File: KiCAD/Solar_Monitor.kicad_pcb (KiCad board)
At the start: 2 copper layers, 40.6 x 22.9 mm, 15 parts, among them J1 Power IN, J2 Power Out, Q1 PN2222A, Q2 MCP102-300E/TO, U1 PIC16F15214-I/P

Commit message: Starting Rev: B
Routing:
- net Net-(C1-Pad1): track 59.3 -> 7.18 mm
- added copper zone on B.Cu, net Net-(C1-Pad1)
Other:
- board text added: "2022-02-16"
- board text added: "Rev: B"
- board text removed: "2022-02-15"
- board text removed: "Rev A"
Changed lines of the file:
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@@
   (net 9 "Net-(Q2-Pad1)")
   (net 10 "Net-(Q2-Pad2)")
-  (net 11 "Net-(U1-Pad7)")
+  (net 11 "Net-(Q1-Pad2)")
   (footprint "MountingHole:MountingHole_2.2mm_M2" (layer "F.Cu")
     (at 83.82 63.5)
@@
       (net 1 "Net-(D1-Pad1)") (pinfunction "Pin_1") (pintype "passive"))
     (pad "2" thru_hole oval (at 0 2.54) (size 1.7 1.7) (drill 1) (layers *.Cu *.Mask)
-      (net 2 "Net-(C1-Pad1)") (pinfunction "Pin_2") (pintype "passive"))
+      (net 2 "Net-(C1-Pad1)") (pinfunction "Pin_2") (pintype "power_out"))
     (model "${KICAD6_3DMODEL_DIR}/Connector_PinHeader_2.54mm.3dshapes/PinHeader_1x02_P2.54mm_Vertical.wrl"
       (offset (xyz 0 0 0))
@@
     (fp_line (start -0.635 -1.27) (end 1.27 -1.27) (layer "F.Fab") (width 0.1))
     (pad "1" thru_hole rect (at 0 0 180) (size 1.7 1.7) (drill 1) (layers *.Cu *.Mask)
-      (net 3 "Net-(C1-Pad2)") (pinfunction "Pin_1") (pintype "passive"))
+      (net 3 "Net-(C1-Pad2)") (pinfunction "Pin_1") (pintype "power_out"))
     (pad "2" thru_hole oval (at 0 2.54 180) (size 1.7 1.7) (drill 1) (layers *.Cu *.Mask)
-      (net 2 "Net-(C1-Pad1)") (pinfunction "Pin_2") (pintype "passive"))
+      (net 2 "Net-(C1-Pad1)") (pinfunction "Pin_2") (pintype "power_in"))
     (model "${KICAD6_3DMODEL_DIR}/Connector_PinHeader_2.54mm.3dshapes/PinHeader_1x02_P2.54mm_Vertical.wrl"
       (offset (xyz 0 0 0))
@@
     (fp_arc (start -0.483625 1.753625) (mid -1.021221 -0.949055) (end 1.27 -2.48) (layer "F.Fab") (width 0.1))
     (pad "1" thru_hole rect (at 0 0) (size 1.3 1.3) (drill 0.75) (layers *.Cu *.Mask)
-      (net 9 "Net-(Q2-Pad1)") (pinfunction "E") (pintype "passive"))
+      (net 9 "Net-(Q2-Pad1)") (pintype "passive"))
     (pad "2" thru_hole circle (at 1.27 -1.27) (size 1.3 1.3) (drill 0.75) (layers *.Cu *.Mask)
-      (net 10 "Net-(Q2-Pad2)") (pinfunction "B") (pintype "passive"))
+      (net 10 "Net-(Q2-Pad2)") (pintype "passive"))
     (pad "3" thru_hole circle (at 2.54 0) (size 1.3 1.3) (drill 0.75) (layers *.Cu *.Mask)
-      (net 2 "Net-(C1-Pad1)") (pinfunction "C") (pintype "passive"))
+      (net 2 "Net-(C1-Pad1)") (pintype "passive"))
     (model "${KICAD6_3DMODEL_DIR}/Package_TO_SOT_THT.3dshapes/TO-92.wrl"
       (offset (xyz 0 0 0))
@@
       (net 8 "Net-(D1-Pad2)") (pinfunction "E") (pintype "passive"))
     (pad "2" thru_hole oval (at 1.27 0 90) (size 1.05 1.5) (drill 0.75) (layers *.Cu *.Mask)
-      (net 11 "Net-(U1-Pad7)") (pinfunction "B") (pintype "input"))
+      (net 11 "Net-(Q1-Pad2)") (pinfunction "B") (pintype "input"))
     (pad "3" thru_hole oval (at 2.54 0 90) (size 1.05 1.5) (drill 0.75) (layers *.Cu *.Mask)
       (net 3 "Net-(C1-Pad2)") (pinfunction "C") (pintype "passive"))
@@
       (net 7 "unconnected-(U1-Pad6)") (pinfunction "RA1/ICSPCLK") (pintype "bidirectional+no_connect"))
     (pad "7" thru_hole oval (at 7.62 2.54) (size 1.6 1.6) (drill 0.8) (layers *.Cu *.Mask)
-      (net 11 "Net-(U1-Pad7)") (pinfunction "RA0/ICSPDAT") (pintype "bidirectional"))
+      (net 11 "Net-(Q1-Pad2)") (pinfunction "RA0/ICSPDAT") (pintype "bidirectional"))
     (pad "8" thru_hole oval (at 7.62 0) (size 1.6 1.6) (drill 0.8) (layers *.Cu *.Mask)
       (net 2 "Net-(C1-Pad1)") (pinfunction "VSS") (pintype "power_in"))
@@
     (effects (font (size 1 1) (thickness 0.15)) (justify left mirror))
   )
-  (gr_text "Rev A" (at 114.3 81.28) (layer "B.SilkS")
+  (gr_text "Rev: B" (at 114.3 81.28) (layer "B.SilkS")
     (effects (font (size 1 1) (thickness 0.15)) (justify left mirror))
   )
-  (gr_text "2022-02-15" (at 101.6 81.28) (layer "B.SilkS")
+  (gr_text "2022-02-16" (at 101.6 81.28) (layer "B.SilkS")
     (effects (font (size 1 1) (thickness 0.15)) (justify left mirror))
   )
@@
   (segment (start 114.3 66.04) (end 116.84 68.58) (width 0.25) (layer "F.Cu") (net 1))
   (segment (start 114.3 66.04) (end 113.03 66.04) (width 0.25) (layer "F.Cu") (net 1))
-  (segment (start 99.06 71.5303) (end 100.165189 72.635489) (width 0.25) (layer "F.Cu") (net 2))
-  (segment (start 106.68 81.28) (end 109.22 78.74) (width 0.25) (layer "F.Cu") (net 2))
-  (segment (start 105.655489 76.2) (end 111.76 76.2) (width 0.25) (layer "F.Cu") (net 2))
-  (segment (start 111.76 76.2) (end 116.84 71.12) (width 0.25) (layer "F.Cu") (net 2))
-  (segment (start 99.06 69.96) (end 99.06 71.5303) (width 0.25) (layer "F.Cu") (net 2))
-  (segment (start 91.44 63.5) (end 94.06 63.5) (width 0.25) (layer "F.Cu") (net 2))
-  (segment (start 86.36 68.58) (end 91.44 63.5) (width 0.25) (layer "F.Cu") (net 2))
-  (segment (start 100.34 68.68) (end 99.06 69.96) (width 0.25) (layer "F.Cu") (net 2))
-  (segment (start 109.22 78.74) (end 111.76 76.2) (width 0.25) (layer "F.Cu") (net 2))
-  (segment (start 83.82 71.12) (end 86.36 68.58) (width 0.25) (layer "F.Cu") (net 2))
-  (segment (start 102.090978 72.635489) (end 105.655489 76.2) (width 0.25) (layer "F.Cu") (net 2))
-  (segment (start 100.165189 72.635489) (end 102.090978 72.635489) (width 0.25) (layer "F.Cu") (net 2))
-  (segment (start 83.82 76.2) (end 83.82 71.12) (width 0.25) (layer "F.Cu") (net 2))
-  (segment (start 94.06 63.5) (end 99.24 68.68) (width 0.25) (layer "B.Cu") (net 2))
-  (segment (start 99.24 68.68) (end 100.34 68.68) (width 0.25) (layer "B.Cu") (net 2))
+  (segment (start 116.84 71.12) (end 111.76 76.2) (width 0.25) (layer "F.Cu") (net 2))
   (segment (start 93.88 68.68) (end 99.06 63.5) (width 0.25) (layer "F.Cu") (net 3))
   (segment (start 105.265787 71.12) (end 106.68 71.12) (width 0.25) (layer "F.Cu") (net 3))
@@
   (segment (start 104.24 71.22) (end 105.41 72.39) (width 0.25) (layer "F.Cu") (net 11))
   (segment (start 100.34 71.22) (end 104.24 71.22) (width 0.25) (layer "F.Cu") (net 11))
+  (zone (net 2) (net_name "Net-(C1-Pad1)") (layer "B.Cu") (name "GND") (hatch edge 0.508)
+    (connect_pads (clearance 0.508))
+    (min_thickness 0.254) (filled_areas_thickness no)
+    (fill yes (thermal_gap 0.508) (thermal_bridge_width 0.508) (smoothing chamfer))
+    (polygon
+      (pts
+        (xy 121.92 83.82)
+        (xy 81.28 83.82)
+        (xy 81.28 60.96)
+        (xy 121.92 60.96)
+      )
+    )
+  )
 )

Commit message: Update Solar_Monitor.kicad_pcb
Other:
- board text added: "TP+"
- board text added: "TP-"
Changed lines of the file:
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@@
       (effects (font (size 1 1) (thickness 0.15)))
     )
-    (fp_text user "K" (at 0 -1.8) (layer "F.SilkS")
+    (fp_text user "K" (at 0 -1.8) (layer "F.SilkS") hide
       (effects (font (size 1 1) (thickness 0.15)))
     )
@@
     (property "Sheetname" "")
     (attr exclude_from_pos_files)
-    (fp_text reference "TP1" (at 0 -2.54) (layer "F.SilkS")
+    (fp_text reference "TP1" (at 0 -2.54) (layer "F.SilkS") hide
       (effects (font (size 1 1) (thickness 0.15)))
     )
@@
     (property "Sheetname" "")
     (attr exclude_from_pos_files)
-    (fp_text reference "TP2" (at 0 -2.54) (layer "F.SilkS")
+    (fp_text reference "TP2" (at 0 -2.54) (layer "F.SilkS") hide
       (effects (font (size 1 1) (thickness 0.15)))
     )
@@
     (effects (font (size 1 1) (thickness 0.15)) (justify left))
   )
+  (gr_text "TP+" (at 95.381351 81.265157) (layer "F.SilkS")
+    (effects (font (size 1 1) (thickness 0.25)))
+  )
+  (gr_text "TP-" (at 112.165664 73.14469) (layer "F.SilkS")
+    (effects (font (size 1 1) (thickness 0.25)))
+  )
   (gr_text "GND" (at 89.317975 68.574225) (layer "F.SilkS")

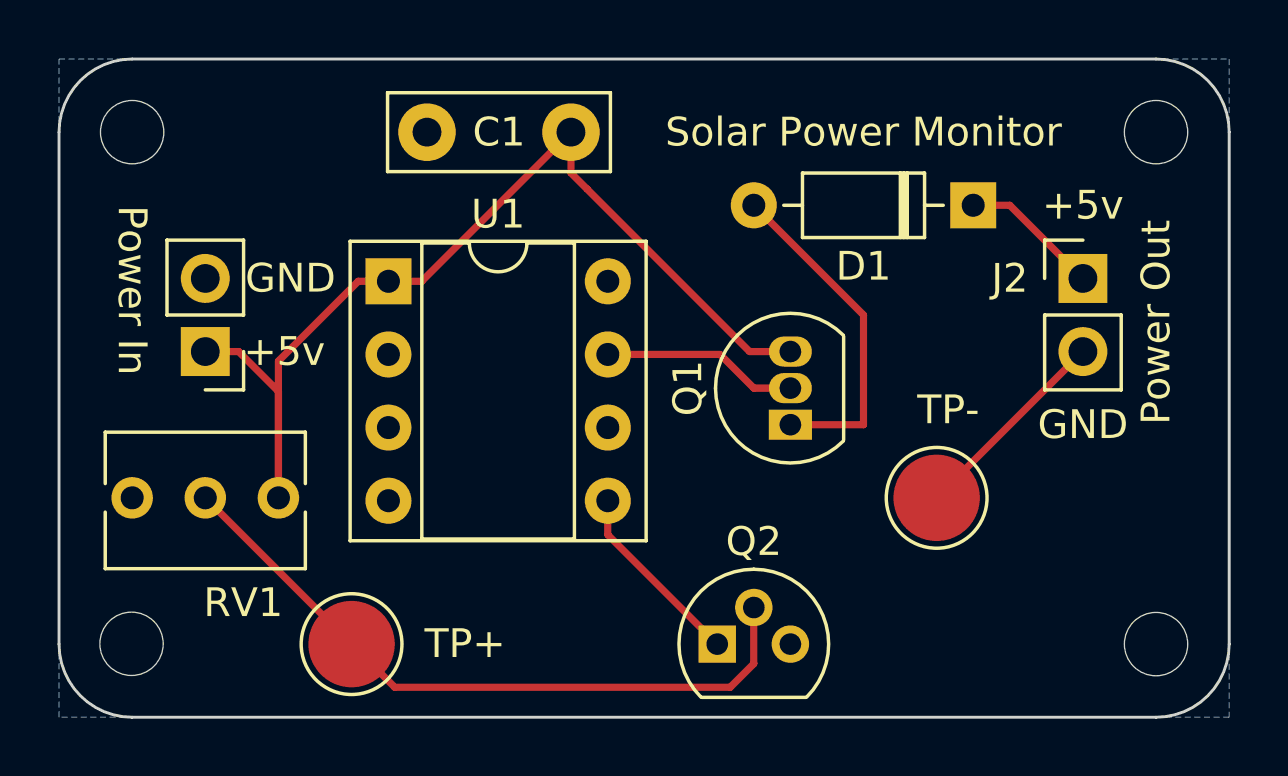
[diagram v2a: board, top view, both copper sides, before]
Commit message: KiCAD: Added button
Added button to reset the output for a set amount of time.
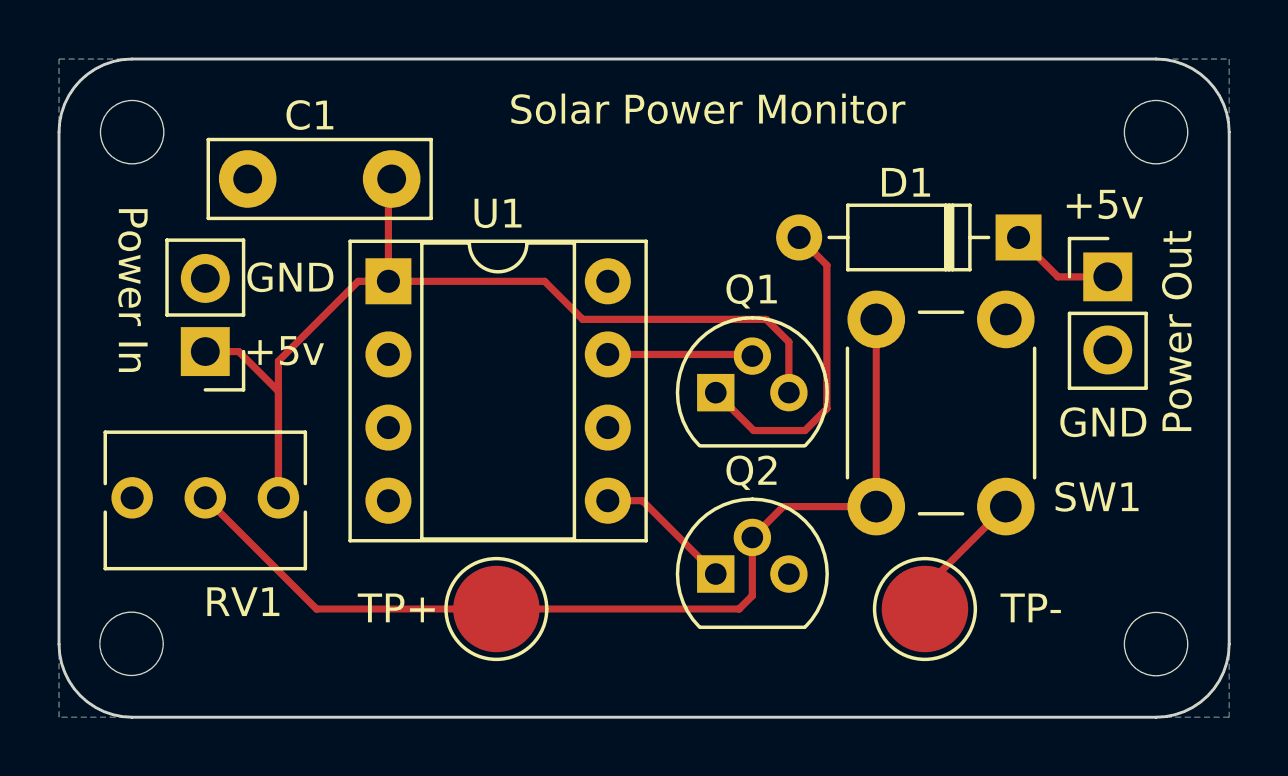
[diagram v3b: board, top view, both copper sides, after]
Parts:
- added SW1: SW_Push, Button_Switch_THT:SW_PUSH_6mm, F.Cu at (114.2, 70.0)
- Q1: footprint Package_TO_SOT_THT:TO-92_Inline -> Package_TO_SOT_THT:TO-92
- moved REF5 16.2 mm to (96.5, 76.5)
- moved C1 6.44 mm to (87.8, 65.1)
- moved TP1 5.17 mm to (96.5, 80.1)
- moved TP2 3.88 mm to (111.4, 80.1)
- moved Q1 2.82 mm to (104.1, 72.5), turned to 0 degrees
- moved Q2 2.43 mm to (104.1, 78.8)
- moved D1 1.93 mm to (114.6, 67.2)
- moved J2 0.87 mm to (117.7, 68.5)
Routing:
- net Net-(Q2-Pad2): track 24.1 -> 34.1 mm
- net Net-(C1-Pad1): track 7.18 -> 4.72 mm
- net Net-(Q2-Pad1): track 6.55 -> 4.80 mm
- net Net-(Q1-Pad2): track 6.82 -> 5.15 mm
- net Net-(D1-Pad1): track 4.86 -> 3.66 mm
- net Net-(D1-Pad2): track 11.7 -> 11.1 mm
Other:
- board text added: "2022-02-22"
- board text added: "github.com/mattrude/solar-monitor"
- board text added: "matt@mattrude.com"
- board text removed: "2022-02-16"
- board text removed: "https://github.com/mattrude/solar-monitor"
- board text removed: "https://mattrude.com"
